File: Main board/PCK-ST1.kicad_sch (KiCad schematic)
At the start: 19 parts

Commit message: As built updated
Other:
- note added: "10k for DRV8434"
- note added: "33k for DRV8434"
- note added: "4k99 for DRV8434"
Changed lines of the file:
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@@
 	(generator_version "9.0")
 	(paper "A4")
+	(text "10k for DRV8434"
+		(exclude_from_sim no)
+		(at 57.912 98.044 0)
+		(effects
+			(font
+				(size 1.27 1.27)
+			)
+		)
+	)
+	(text "10k for DRV8434"
+		(exclude_from_sim no)
+		(at 56.896 63.246 0)
+		(effects
+			(font
+				(size 1.27 1.27)
+			)
+		)
+	)
+	(text "33k for DRV8434"
+		(exclude_from_sim no)
+		(at 58.42 160.528 0)
+		(effects
+			(font
+				(size 1.27 1.27)
+			)
+		)
+	)
+	(text "4k99 for DRV8434"
+		(exclude_from_sim no)
+		(at 58.42 170.942 0)
+		(effects
+			(font
+				(size 1.27 1.27)
+			)
+		)
+	)
+	(text "10k for DRV8434"
+		(exclude_from_sim no)
+		(at 58.166 133.858 0)
+		(effects
+			(font
+				(size 1.27 1.27)
+			)
+		)
+	)
 	(junction
 		(at 68.58 165.1)

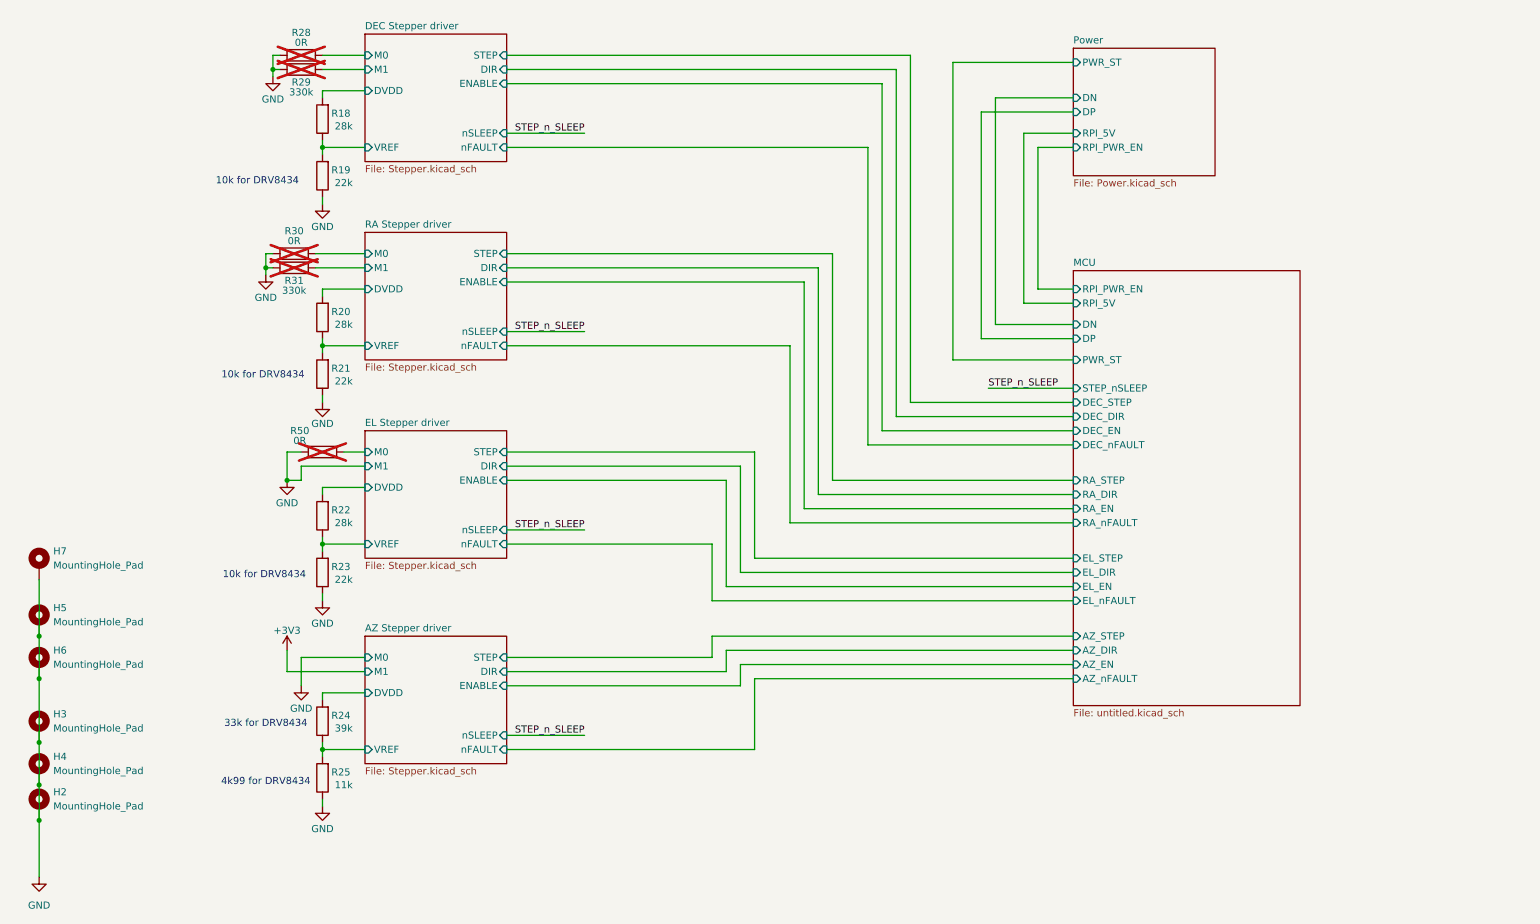
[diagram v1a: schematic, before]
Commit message: Main board updated to v0.3
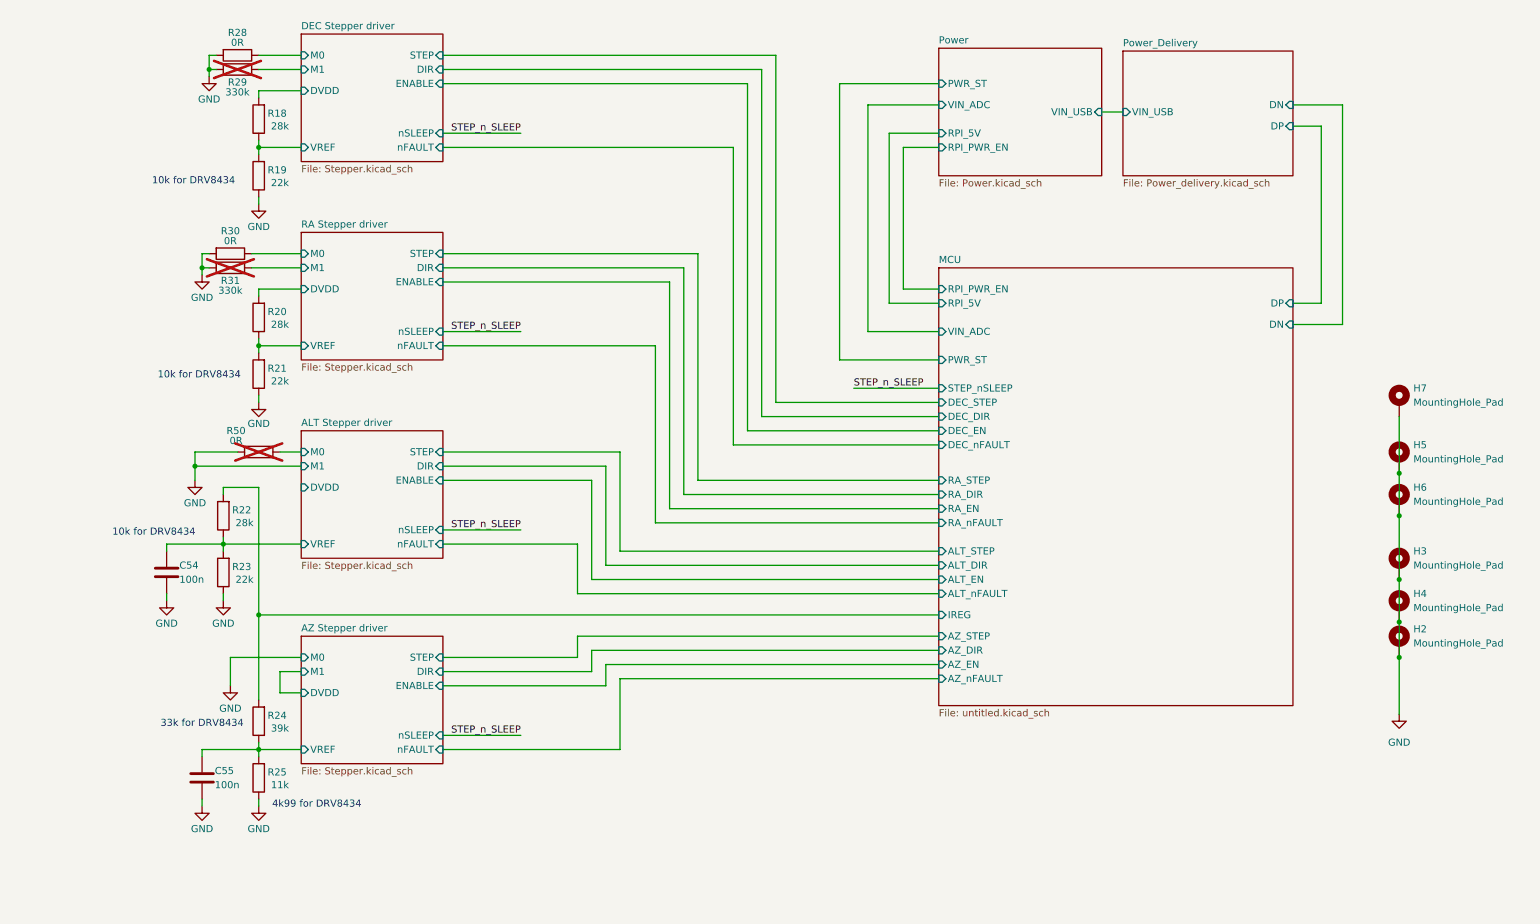
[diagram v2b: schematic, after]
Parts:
- added C54, C55: 100n, Capacitor_SMD:C_0402_1005Metric, symbol Device:C
- R28, R30: now fitted
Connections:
- net AZ Stepper driver/DVDD: no longer R24.2
- net AZ Stepper driver/VREF: now also C55.1
- net ALT Stepper driver/DVDD: no longer R22.2
- net ALT Stepper driver/VREF: now also C54.1
- net GND: now also C54.2, C55.2
- new net MCU/IREG: R22.2, R24.2
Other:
- sheet EL Stepper driver renamed ALT Stepper driver
- added sheet Power_Delivery (Power_delivery.kicad_sch)
- sheet MCU ports: added ALT_DIR, ALT_EN, ALT_STEP, ALT_nFAULT, IREG, VIN_ADC; removed EL_DIR, EL_EN, EL_STEP, EL_nFAULT
- sheet Power ports: added VIN_ADC, VIN_USB; removed DN, DP
- moved on the sheet: H2, H3, H4, H5, H6, H7, R18, R19, R20, R21, R22, R23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

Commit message: schema updated
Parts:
- R19, R21, R23: value 22k -> 10k
- R22: value 28k -> 20k
- R24: value 39k -> 47k
- R25: value 11k -> 10k
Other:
- moved on the sheet: C54, C55, R18, R19, R20, R21, R22, R23, R24, R25, R28, R29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

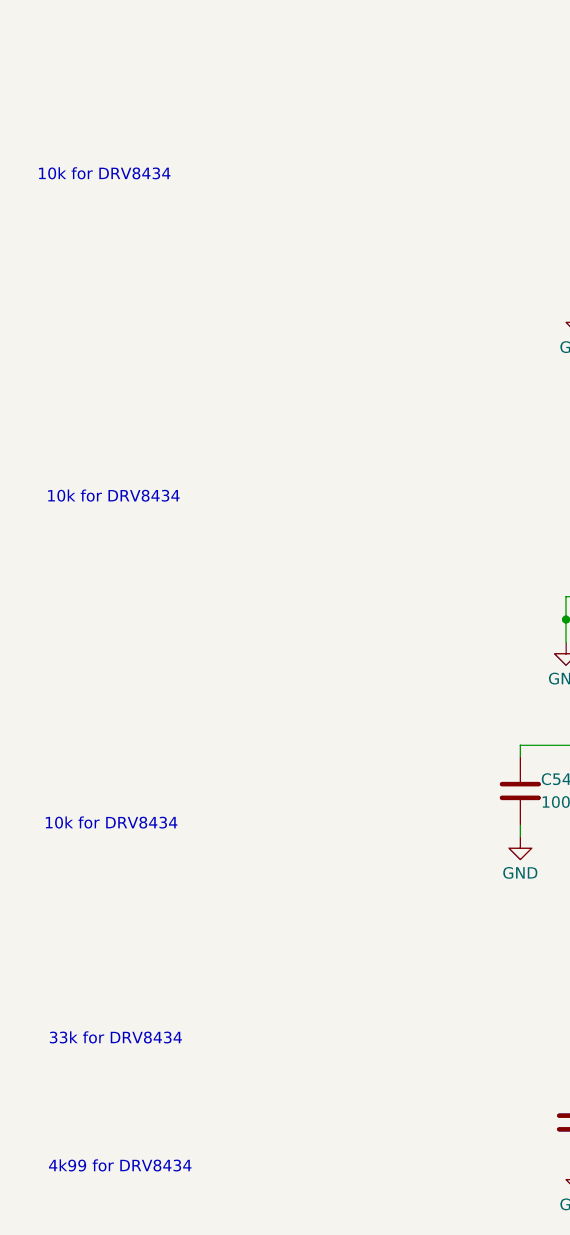
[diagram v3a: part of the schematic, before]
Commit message: Main board updated to v0.3
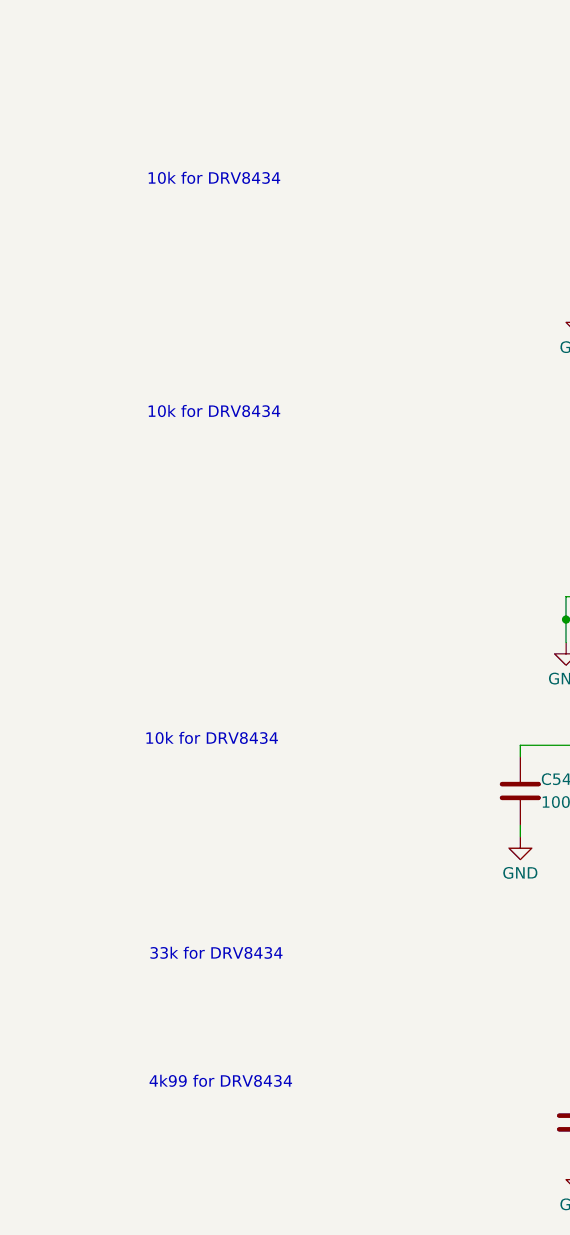
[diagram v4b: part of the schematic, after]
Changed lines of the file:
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@@
 	(text "10k for DRV8434"
 		(exclude_from_sim no)
-		(at 23.368 99.568 0)
+		(at 34.544 90.17 0)
 		(effects
 			(font
@@
 	(text "10k for DRV8434"
 		(exclude_from_sim no)
-		(at 22.352 63.754 0)
+		(at 34.544 64.262 0)
 		(effects
 			(font
@@
 	(text "33k for DRV8434"
 		(exclude_from_sim no)
-		(at 23.622 159.766 0)
+		(at 34.798 150.368 0)
 		(effects
 			(font
@@
 	(text "4k99 for DRV8434"
 		(exclude_from_sim no)
-		(at 24.13 173.99 0)
+		(at 35.306 164.592 0)
 		(effects
 			(font
@@
 	(text "10k for DRV8434"
 		(exclude_from_sim no)
-		(at 23.114 135.89 0)
+		(at 34.29 126.492 0)
 		(effects
 			(font

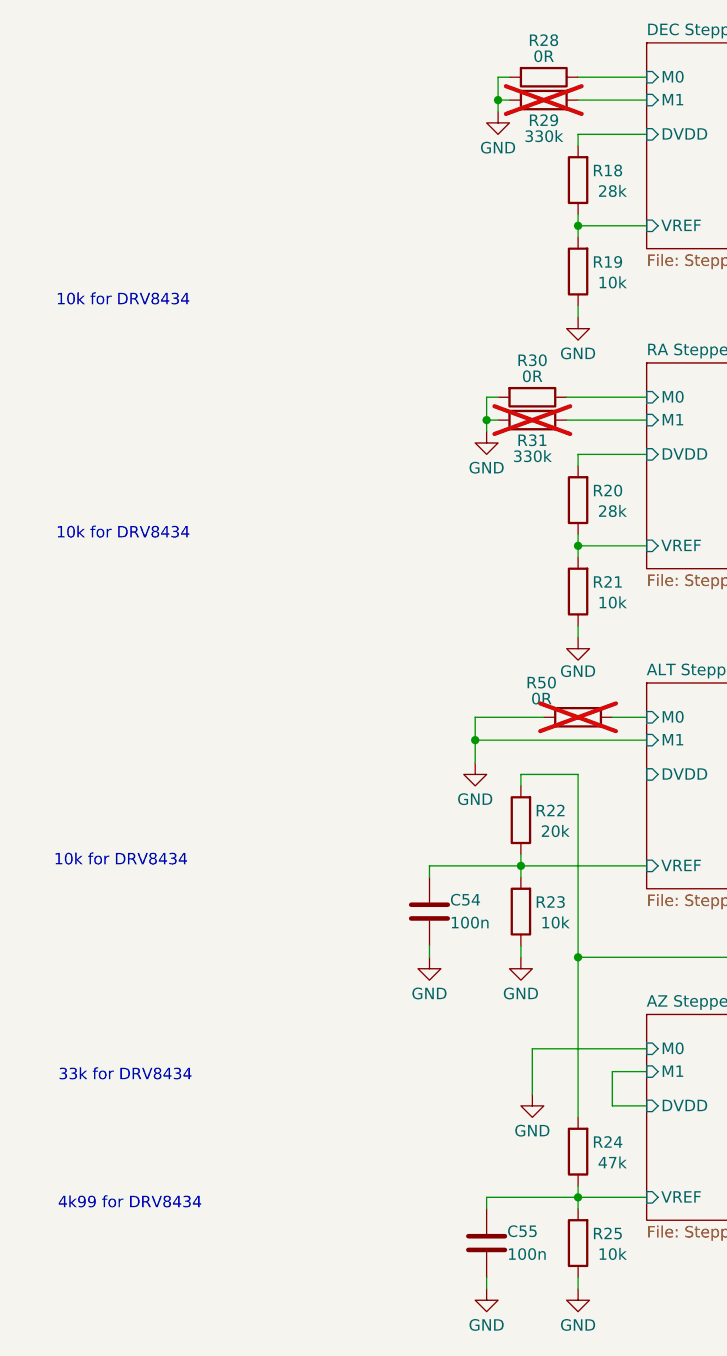
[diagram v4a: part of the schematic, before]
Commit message: Added part numbers for simpler ordering
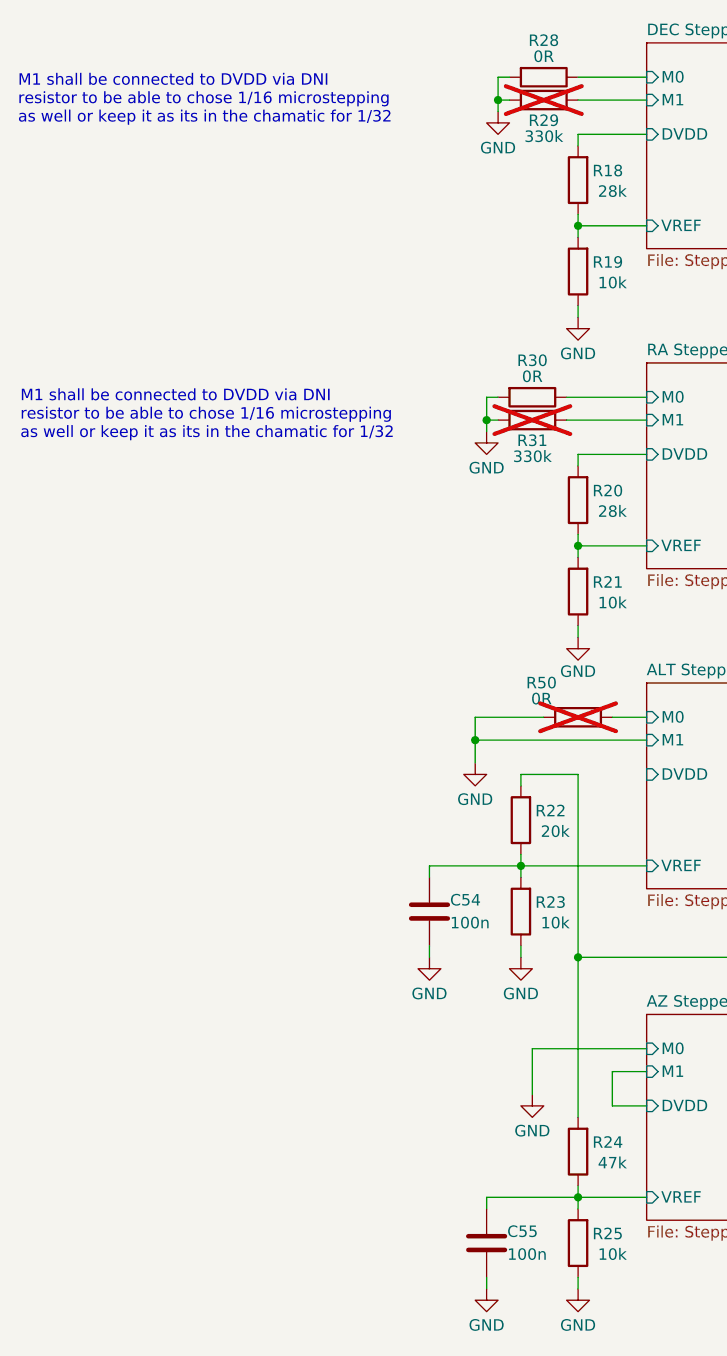
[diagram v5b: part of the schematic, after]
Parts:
- C54, C55: Part Number (none) -> GRM155R71C104JA88D
- R18, R20: Part Number (none) -> CRCW040228K0FKED
- R19, R21, R23, R25: Part Number (none) -> CRCW040210K0FKEDC
- R22: Part Number (none) -> CRCW040220K0FKEDHP
- R24: Part Number (none) -> CRCW040247K0FKED
- R28, R30, R50: Part Number (none) -> CRCW04020000Z0EDC
- R29, R31: Part Number (none) -> CRCW0402330KFKED
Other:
- note added: "M1 shall be connected to DVDD via DNI resistor to be able to chose 1/16 microstepping as well or keep it as its in the chamatic for 1/32"
- note removed: "10k for DRV8434"
- note removed: "33k for DRV8434"
- note removed: "4k99 for DRV8434"
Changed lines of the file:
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@@
 	(generator_version "9.0")
 	(paper "A4")
-	(text "10k for DRV8434"
+	(text "M1 shall be connected to DVDD via DNI\nresistor to be able to chose 1/16 microstepping\nas well or keep it as its in the chamatic for 1/32"
 		(exclude_from_sim no)
-		(at 34.544 90.17 0)
+		(at 23.114 76.962 0)
 		(effects
 			(font
 				(size 1.27 1.27)
+				(color 255 21 1 1)
 			)
+			(justify left)
 		)
 	)
-	(text "10k for DRV8434"
+	(text "M1 shall be connected to DVDD via DNI\nresistor to be able to chose 1/16 microstepping\nas well or keep it as its in the chamatic for 1/32"
 		(exclude_from_sim no)
-		(at 34.544 64.262 0)
-		(effects
-			(font
-				(size 1.27 1.27)
-			)
-		)
-	)
-	(text "33k for DRV8434"
-		(exclude_from_sim no)
-		(at 34.798 150.368 0)
-		(effects
-			(font
-				(size 1.27 1.27)
-			)
-		)
-	)
-	(text "4k99 for DRV8434"
-		(exclude_from_sim no)
-		(at 35.306 164.592 0)
-		(effects
-			(font
-				(size 1.27 1.27)
-			)
-		)
-	)
-	(text "10k for DRV8434"
-		(exclude_from_sim no)
-		(at 34.29 126.492 0)
+		(at 22.86 41.91 0)
 		(effects
 			(font
 				(size 1.27 1.27)
+				(color 255 21 1 1)
 			)
+			(justify left)
 		)
 	)
@@
 			)
 		)
+		(property "Part Number" "CRCW0402330KFKED"
+			(at 81.28 41.91 0)
+			(effects
+				(font
+					(size 1.27 1.27)
+				)
+				(hide yes)
+			)
+		)
 		(pin "2"
 		)
@@
 			)
 		)
+		(property "Part Number" "CRCW040228K0FKED"
+			(at 85.09 50.8 0)
+			(effects
+				(font
+					(size 1.27 1.27)
+				)
+				(hide yes)
+			)
+		)
 		(pin "2"
 		)
@@
 			)
 		)
+		(property "Part Number" "CRCW040210K0FKEDC"
+			(at 78.74 132.08 0)
+			(effects
+				(font
+					(size 1.27 1.27)
+				)
+				(hide yes)
+			)
+		)
 		(pin "2"
 		)
@@
 			)
 		)
+		(property "Part Number" "GRM155R71C104JA88D"
+			(at 68.326 130.302 0)
+			(effects
+				(font
+					(size 1.27 1.27)
+				)
+				(hide yes)
+			)
+		)
 		(pin "2"
 		)
@@
 			)
 		)
+		(property "Part Number" ""
+			(at 261.62 113.03 0)
+			(effects
+				(font
+					(size 1.27 1.27)
+				)
+			)
+		)
 		(pin "1"
 		)
@@
 			)
 		)
+		(property "Part Number" "CRCW040220K0FKEDHP"
+			(at 78.74 121.92 0)
+			(effects
+				(font
+					(size 1.27 1.27)
+				)
+				(hide yes)
+			)
+		)
 		(pin "2"
 		)
@@
 			)
 		)
+		(property "Part Number" "CRCW04020000Z0EDC"
+			(at 80.01 74.93 0)
+			(effects
+				(font
+					(size 1.27 1.27)
+				)
+				(hide yes)
+			)
+		)
 		(pin "2"
 		)
@@
 			)
 		)
+		(property "Part Number" "CRCW04020000Z0EDC"
+			(at 85.09 110.49 0)
+			(effects
+				(font
+					(size 1.27 1.27)
+				)
+				(hide yes)
+			)
+		)
 		(pin "2"
 		)
@@
 			)
 		)
+		(property "Part Number" ""
+			(at 261.62 139.7 0)
+			(effects
+				(font
+					(size 1.27 1.27)
+				)
+			)
+		)
 		(pin "1"
 		)
@@
 			)
 		)
+		(property "Part Number" ""
+			(at 261.62 120.65 0)
+			(effects
+				(font
+					(size 1.27 1.27)
+				)
+			)
+		)
 		(pin "1"
 		)
@@
 			)
 		)
+		(property "Part Number" "CRCW04020000Z0EDC"
+			(at 81.28 39.37 0)
+			(effects
+				(font
+					(size 1.27 1.27)
+				)
+				(hide yes)
+			)
+		)
 		(pin "2"
 		)
@@
 			)
 		)
+		(property "Part Number" "CRCW0402330KFKED"
+			(at 80.01 77.47 0)
+			(effects
+				(font
+					(size 1.27 1.27)
+				)
+				(hide yes)
+			)
+		)
 		(pin "2"
 		)
@@
 			)
 		)
+		(property "Part Number" "GRM155R71C104JA88D"
+			(at 74.676 164.846 0)
+			(effects
+				(font
+					(size 1.27 1.27)
+				)
+				(hide yes)
+			)
+		)
 		(pin "2"
 		)
@@
 			)
 		)
+		(property "Part Number" ""
+			(at 261.62 146.05 0)
+			(effects
+				(font
+					(size 1.27 1.27)
+				)
+			)
+		)
 		(pin "1"
 		)
@@
 			)
 		)
+		(property "Part Number" ""
+			(at 261.62 102.87 0)
+			(effects
+				(font
+					(size 1.27 1.27)
+				)
+			)
+		)
 		(pin "1"
 		)
@@
 			)
 		)
+		(property "Part Number" "CRCW040210K0FKEDC"
+			(at 85.09 96.52 0)
+			(effects
+				(font
+					(size 1.27 1.27)
+				)
+				(hide yes)
+			)
+		)
 		(pin "2"
 		)
@@
 			)
 		)
+		(property "Part Number" "CRCW040210K0FKEDC"
+			(at 85.09 168.91 0)
+			(effects
+				(font
+					(size 1.27 1.27)
+				)
+				(hide yes)
+			)
+		)
 		(pin "2"
 		)
@@
 			)
 		)
+		(property "Part Number" ""
+			(at 261.62 132.08 0)
+			(effects
+				(font
+					(size 1.27 1.27)
+				)
+			)
+		)
 		(pin "1"
 		)
@@
 			)
 		)
+		(property "Part Number" "CRCW040228K0FKED"
+			(at 85.09 86.36 0)
+			(effects
+				(font
+					(size 1.27 1.27)
+				)
+				(hide yes)
+			)
+		)
 		(pin "2"
 		)
@@
 			)
 		)
+		(property "Part Number" "CRCW040210K0FKEDC"
+			(at 85.09 60.96 0)
+			(effects
+				(font
+					(size 1.27 1.27)
+				)
+				(hide yes)
+			)
+		)
 		(pin "2"
 		)
@@
 			(at 85.09 158.75 0)
 			(effects
+				(font
+					(size 1.27 1.27)
+				)
+				(hide yes)
+			)
+		)
+		(property "Part Number" "CRCW040247K0FKED"
+			(at 85.09 158.75 0)
+			(effects

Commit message: Updated Main board to v1.0
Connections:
- net DEC Stepper driver/DVDD: now also R29.1
- net GND: no longer R29.1, R31.1
- net RA Stepper driver/DVDD: now also R31.1
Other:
- note removed: "M1 shall be connected to DVDD via DNI resistor to be able to chose 1/16 microstepping as well or keep it as its in the chamatic for 1/32"
- moved on the sheet: R28, R29, R30, R31
